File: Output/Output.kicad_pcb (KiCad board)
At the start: 2 copper layers, 109 x 52.9 mm, 18 parts, among them J1 Conn_01x10_Pin, J2 Conn_01x04_Pin, U1 74LS173, U2 74LS173, U3 AT28C64B-15PI, U4 CC56-12CGKWA, U5 NE555P, U6 CD74HCT139E, U7 CD74HCT73E

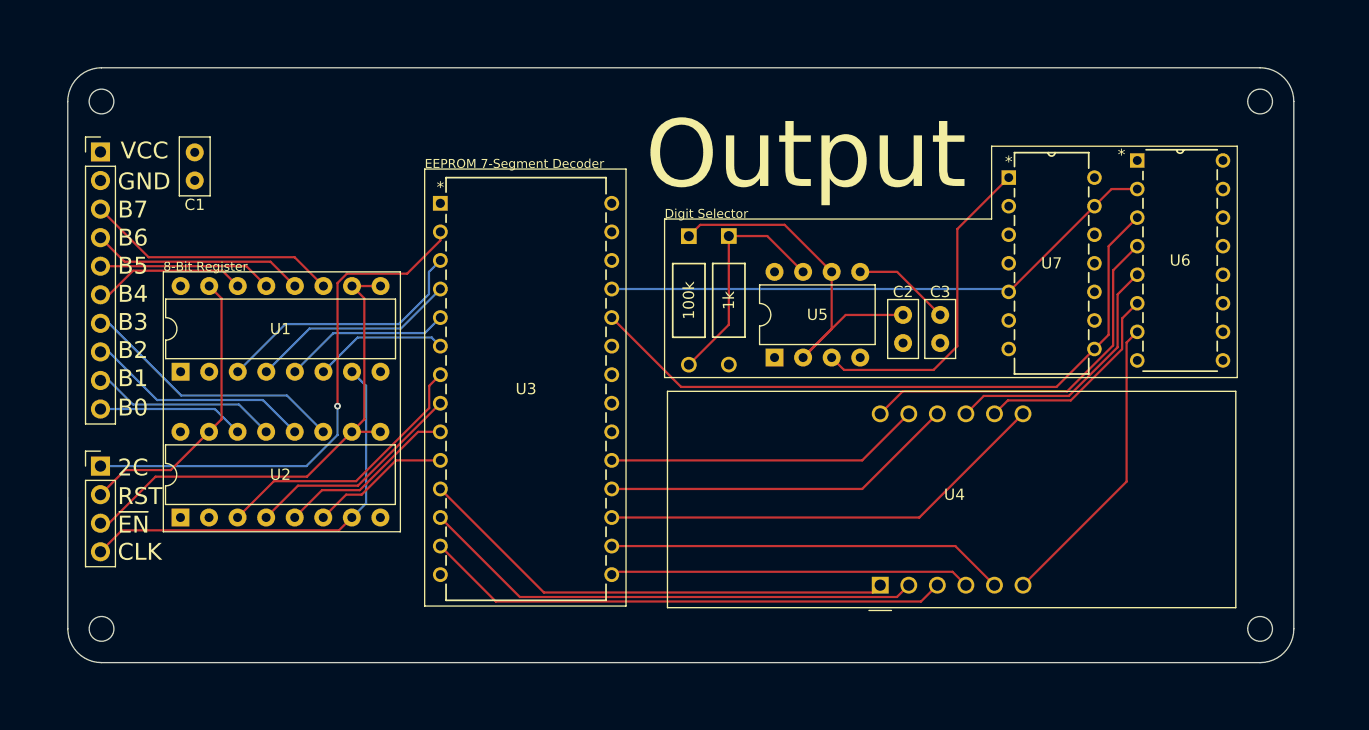
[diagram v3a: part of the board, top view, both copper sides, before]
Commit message: Shrank board size
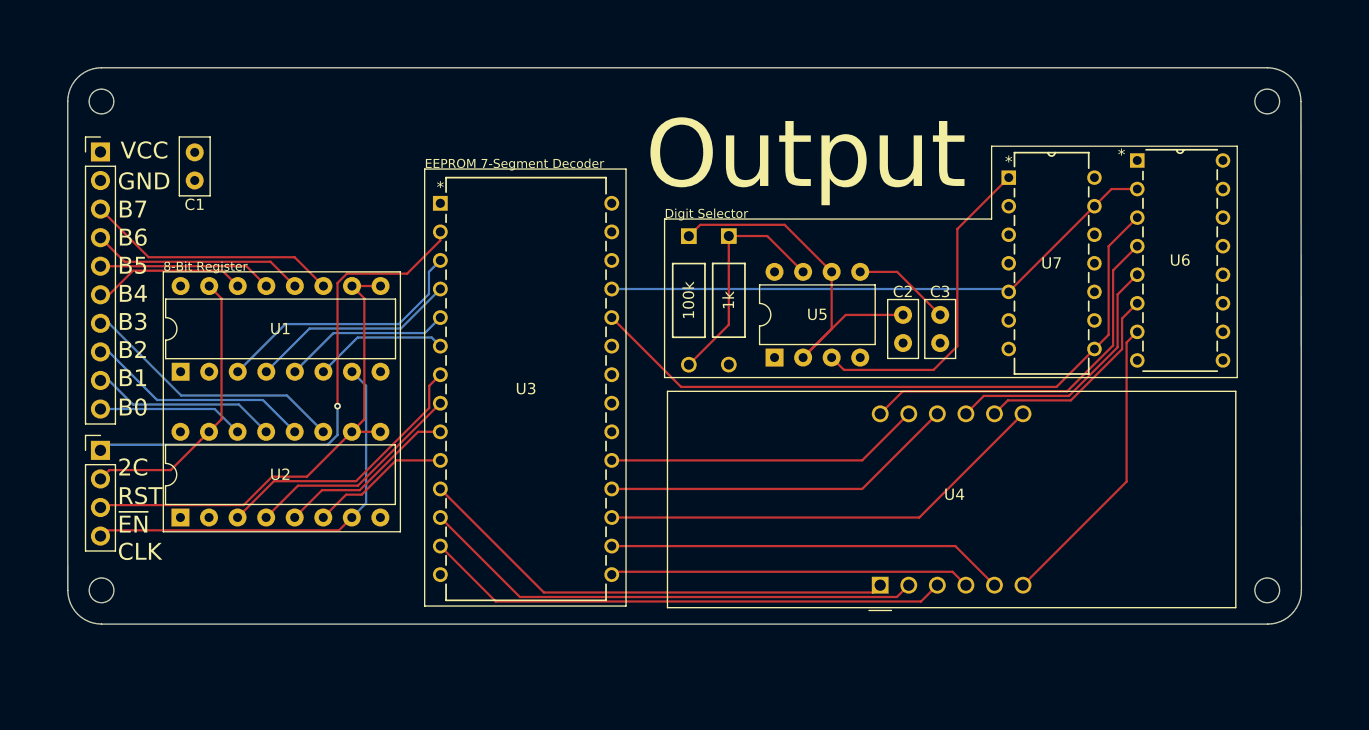
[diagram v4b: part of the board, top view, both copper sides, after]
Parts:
- moved REF** 3.49 mm to (194.2, 110.4)
- moved REF** 3.43 mm to (90.5, 110.4)
- moved J2 1.40 mm to (90.4, 97.9)
- moved REF** 0.64 mm to (194.2, 66.9)
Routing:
- net /~{En}: track 44.7 -> 44.1 mm
- net /RST: track 25.8 -> 25.3 mm
- net /CLK: track 37.6 -> 37.0 mm
- net /2's Comp: track 47.2 -> 46.6 mm
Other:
- board size 109 x 52.9 mm -> 109.7 x 49.5 mm
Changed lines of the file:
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@@
 	(footprint "Connector_PinHeader_2.54mm:PinHeader_1x04_P2.54mm_Vertical"
 		(layer "F.Cu")
-		(at 90.424 99.314)
+		(at 90.424 97.917)
 		(descr "Through hole straight pin header, 1x04, 2.54mm pitch, single row")
 		(tags "Through hole pin header THT 1x04 2.54mm single row")
@@
 	(footprint "MountingHole:MountingHole_2.2mm_M2"
 		(layer "F.Cu")
-		(at 90.52 113.79 90)
+		(at 90.52 110.363001 90)
 		(descr "Mounting Hole 2.2mm, no annular, M2")
 		(tags "mounting hole 2.2mm no annular m2")
@@
 	(footprint "MountingHole:MountingHole_2.2mm_M2"
 		(layer "F.Cu")
-		(at 193.548 66.89132 -90)
+		(at 194.183 66.889319 -90)
 		(descr "Mounting Hole 2.2mm, no annular, M2")
 		(tags "mounting hole 2.2mm no annular m2")
@@
 	(footprint "MountingHole:MountingHole_2.2mm_M2"
 		(layer "F.Cu")
-		(at 193.548 113.792 180)
+		(at 194.183 110.363 180)
 		(descr "Mounting Hole 2.2mm, no annular, M2")
 		(tags "mounting hole 2.2mm no annular m2")
@@
 	)
 	(gr_arc
-		(start 90.52 116.79)
-		(mid 88.39868 115.91132)
-		(end 87.52 113.79)
+		(start 90.52 113.363001)
+		(mid 88.39868 112.484321)
+		(end 87.52 110.363001)
 		(stroke
 			(width 0.05)
@@
 	(gr_line
 		(start 87.51332 66.89132)
-		(end 87.52 113.79)
+		(end 87.52 110.363001)
 		(stroke
 			(width 0.05)
@@
 	)
 	(gr_line
-		(start 90.52 116.79)
-		(end 193.548 116.792)
+		(start 90.52 113.363001)
+		(end 194.22068 113.365001)
 		(stroke
 			(width 0.05)
@@
 	)
 	(gr_line
-		(start 196.548 113.792)
-		(end 196.548 66.89132)
+		(start 197.22068 110.365001)
+		(end 197.183 66.889319)
 		(stroke
 			(width 0.05)
@@
 	)
 	(gr_line
-		(start 193.548 63.89132)
+		(start 194.183 63.889319)
 		(end 90.51332 63.89132)
 		(stroke
@@
 	)
 	(gr_arc
-		(start 193.548 63.89132)
-		(mid 195.66932 64.77)
-		(end 196.548 66.89132)
+		(start 194.183 63.889319)
+		(mid 196.30432 64.767999)
+		(end 197.183 66.889319)
 		(stroke
 			(width 0.05)
@@
 	)
 	(gr_arc
-		(start 196.548 113.792)
-		(mid 195.66932 115.91332)
-		(end 193.548 116.792)
+		(start 197.22068 110.365001)
+		(mid 196.342 112.486321)
+		(end 194.22068 113.365001)
 		(stroke
 			(width 0.05)
@@
 	)
 	(segment
-		(start 90.424 101.854)
-		(end 92.6084 99.6696)
+		(start 90.424 100.457)
+		(end 91.2114 99.6696)
 		(width 0.2)
 		(layer "F.Cu")
@@
 	)
 	(segment
-		(start 92.6084 99.6696)
-		(end 96.6724 99.6696)
+		(start 96.6724 99.6696)
+		(end 100.076 96.266)
 		(width 0.2)
 		(layer "F.Cu")
@@
 	)
 	(segment
-		(start 96.6724 99.6696)
-		(end 100.076 96.266)
+		(start 100.091 83.302)
+		(end 101.191 84.402)
 		(width 0.2)
 		(layer "F.Cu")
@@
 	)
 	(segment
-		(start 100.091 83.302)
-		(end 101.191 84.402)
+		(start 91.2114 99.6696)
+		(end 96.6724 99.6696)
 		(width 0.2)
 		(layer "F.Cu")
@@
 	)
 	(segment
-		(start 90.424 106.934)
-		(end 92.329 105.029)
+		(start 90.932 105.029)
+		(end 111.633 105.029)
 		(width 0.2)
 		(layer "F.Cu")
@@
 	)
 	(segment
-		(start 92.329 105.029)
-		(end 111.633 105.029)
+		(start 90.424 105.537)
+		(end 90.932 105.029)
 		(width 0.2)
 		(layer "F.Cu")
@@
 	(segment
 		(start 108.788 100.254)
-		(end 112.776 96.266)
+		(end 105.682314 100.254)
 		(width 0.2)
 		(layer "F.Cu")
@@
 	)
 	(segment
-		(start 91.186 104.394)
-		(end 95.326 100.254)
+		(start 103.150314 102.786)
+		(end 90.635 102.786)
 		(width 0.2)
 		(layer "F.Cu")
@@
 	)
 	(segment
-		(start 115.331 83.302)
-		(end 112.791 83.302)
+		(start 112.776 96.266)
+		(end 108.788 100.254)
 		(width 0.2)
 		(layer "F.Cu")
@@
 	)
 	(segment
-		(start 95.326 100.254)
-		(end 108.788 100.254)
+		(start 115.331 83.302)
+		(end 112.791 83.302)
 		(width 0.2)
 		(layer "F.Cu")
@@
 	)
 	(segment
-		(start 90.424 104.394)
-		(end 91.186 104.394)
+		(start 105.682314 100.254)
+		(end 103.150314 102.786)
+		(width 0.2)
+		(layer "F.Cu")
+		(net 15)
+	)
+	(segment
+		(start 90.635 102.786)
+		(end 90.424 102.997)
 		(width 0.2)
 		(layer "F.Cu")
@@
 	)
 	(segment
-		(start 108.743635 99.314)
-		(end 111.506 96.551635)
+		(start 90.932 97.409)
+		(end 110.648635 97.409)
 		(width 0.2)
 		(layer "B.Cu")
@@
 	)
 	(segment
-		(start 111.506 96.551635)
-		(end 111.506 93.98)
+		(start 90.424 97.917)
+		(end 90.932 97.409)
 		(width 0.2)
 		(layer "B.Cu")
@@
 	)
 	(segment
-		(start 90.424 99.314)
-		(end 108.743635 99.314)
+		(start 110.648635 97.409)
+		(end 111.506 96.551635)
+		(width 0.2)
+		(layer "B.Cu")
+		(net 16)
+	)
+	(segment
+		(start 111.506 96.551635)
+		(end 111.506 93.98)
 		(width 0.2)
 		(layer "B.Cu")
